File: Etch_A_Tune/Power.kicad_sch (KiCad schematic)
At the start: 2 parts, among them IC4 LM2775DSGR, IC5 TPS62063DSGR

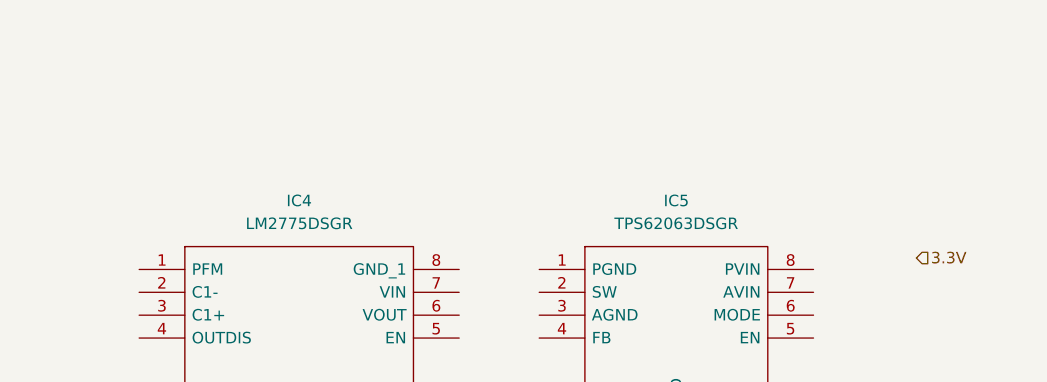
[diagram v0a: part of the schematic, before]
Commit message: Updated schematic and preliminary PCB doc
did rough PCB layout
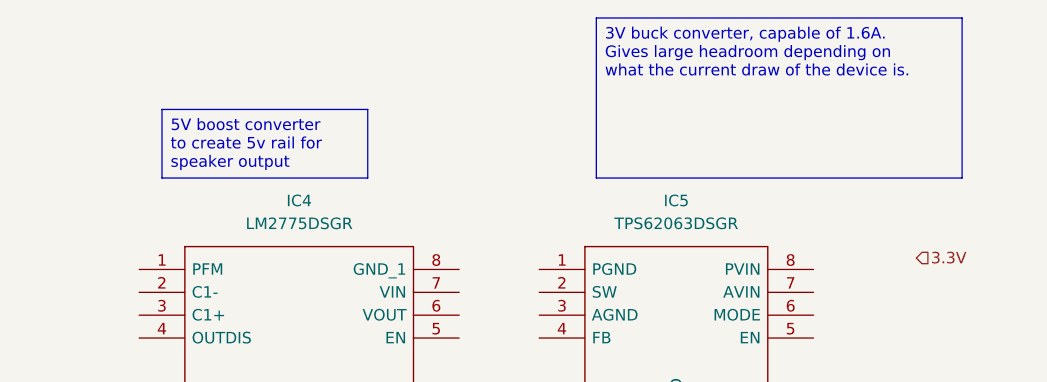
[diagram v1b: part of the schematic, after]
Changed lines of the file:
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@@
 	(generator_version "9.0")
 	(paper "A4")
+	(text_box "3V buck converter, capable of 1.6A. Gives large headroom depending on what the current draw of the device is.\n"
+		(exclude_from_sim no)
+		(at 190.5 50.8 0)
+		(size 40.64 17.78)
+		(margins 0.9525 0.9525 0.9525 0.9525)
+		(stroke
+			(width 0)
+			(type solid)
+		)
+		(fill
+			(type none)
+		)
+		(effects
+			(font
+				(size 1.27 1.27)
+			)
+			(justify left top)
+		)
+	)
+	(text_box "5V boost converter to create 5v rail for speaker output\n"
+		(exclude_from_sim no)
+		(at 142.24 60.96 0)
+		(size 22.86 7.62)
+		(margins 0.9525 0.9525 0.9525 0.9525)
+		(stroke
+			(width 0)
+			(type solid)
+		)
+		(fill
+			(type none)
+		)
+		(effects
+			(font
+				(size 1.27 1.27)
+			)
+			(justify left top)
+		)
+	)
 	(hierarchical_label "3.3V"
 		(shape input)

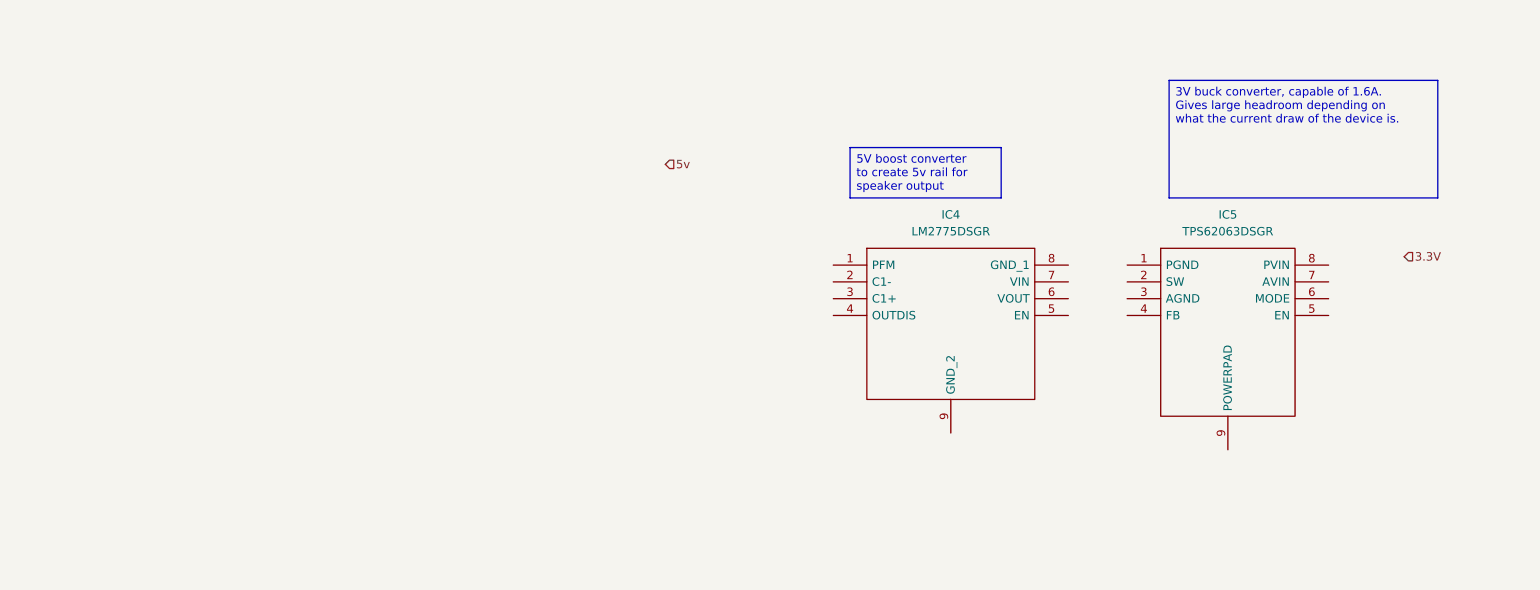
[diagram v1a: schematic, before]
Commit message: Schematic Update
Fixed component Footprints and added new switches/rotary encoders. Wired and placed bypass capacitors for most devices. Removed 5V boost converter because external DAC is no longer being utilized. Placed uC onto board design and implemented charging through USB-C connector.
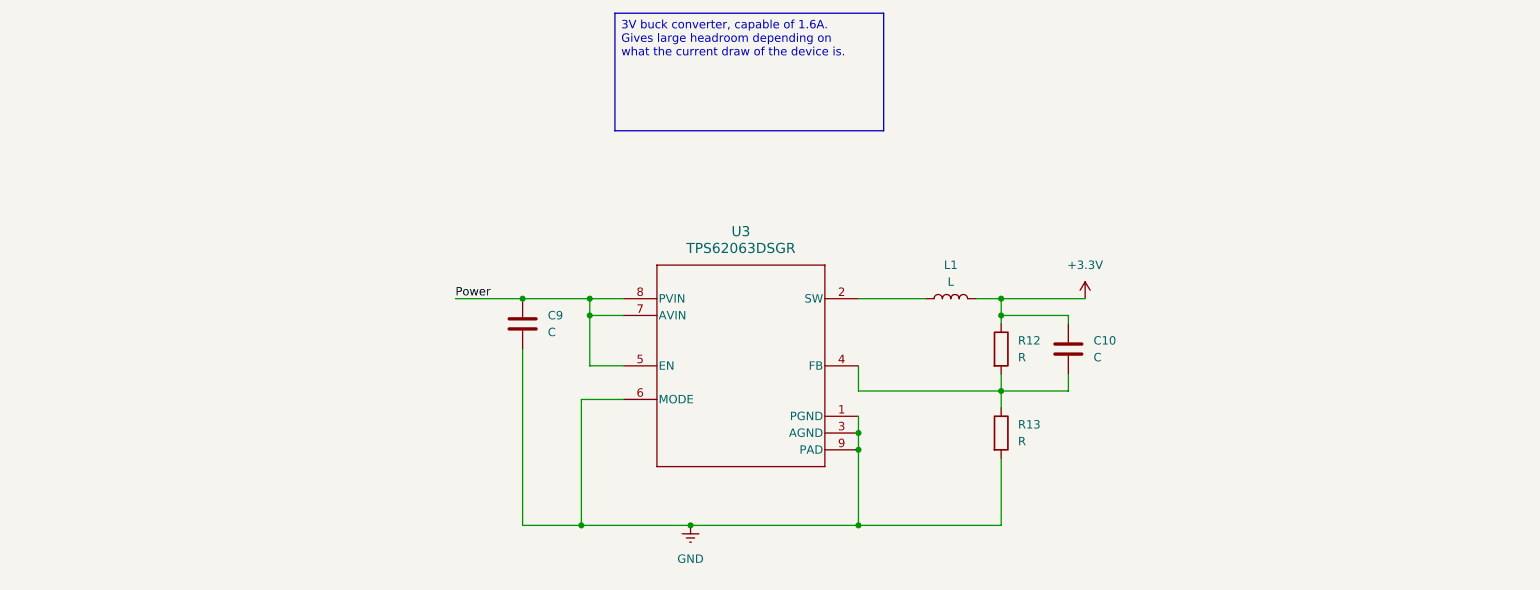
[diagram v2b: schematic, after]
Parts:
- removed IC4: LM2775DSGR, SON50P200X200X80-9N, symbol SamacSys_Parts:LM2775DSGR
- removed IC5: TPS62063DSGR, SON50P200X200X80-9N, symbol SamacSys_Parts:TPS62063DSGR
- added C10, C9: C, symbol Device:C
- added L1: L, symbol Device:L
- added R12, R13: R, symbol Device:R
- added U3: TPS62063DSGR, BQ25170DSGR:DSG0008A, symbol TPS62063DSGR:TPS62063DSGR
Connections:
- new net: L1.1, U3.2 (SW)
- new net: C10.2, R12.2, R13.1, U3.4 (FB)
- new net +3.3V: C10.1, L1.2, R12.1
- new net GND: C9.2, R13.2, U3.1 (PGND), U3.3 (AGND), U3.6 (MODE), U3.9 (PAD)
- new net Power: C9.1, U3.5 (EN), U3.7 (AVIN), U3.8 (PVIN)

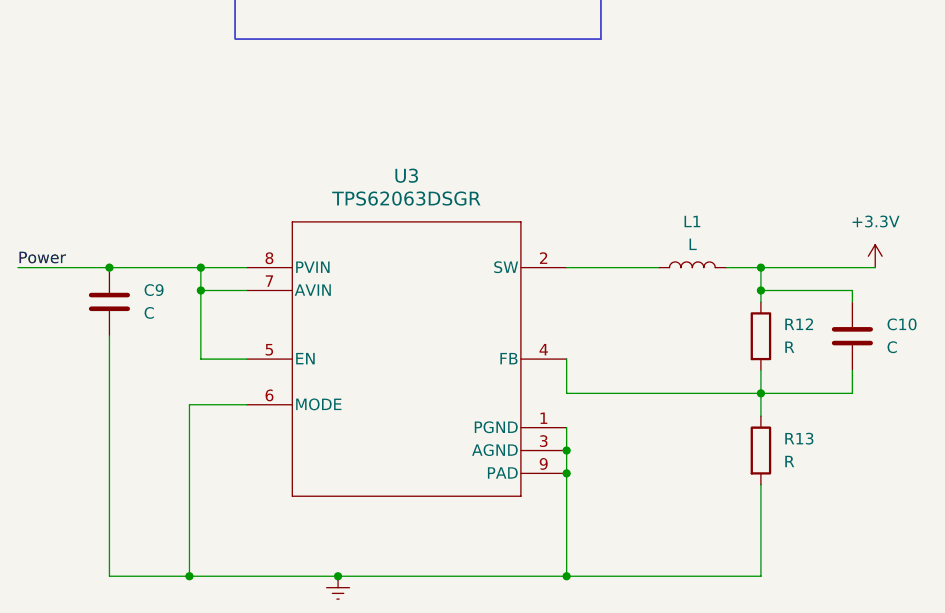
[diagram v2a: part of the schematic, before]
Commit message: Etch A Tune V.02
Updated more foot prints and components onto bom, specifically SWD debug header and 1x14 pin header for touch and screen module. Added 4pin header for SD card reader.
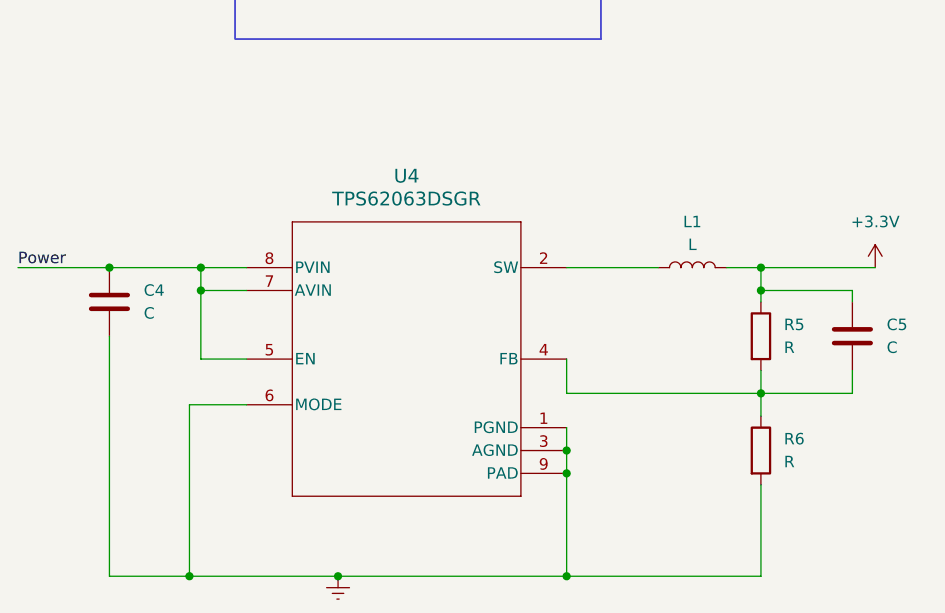
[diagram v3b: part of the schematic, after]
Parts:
- renumbered C9 to C4, C10 to C5, R12 to R5, R13 to R6, U3 to U4
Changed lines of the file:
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@@
 		(dnp no)
 		(fields_autoplaced yes)
-		(property "Reference" "C9"
+		(property "Reference" "C4"
 			(at 96.52 86.3599 0)
 			(effects
@@
 			(project "Etch_A_Tune"
 				(path "/b4cdadf2-c4fe-48fe-ba6a-e15d1cad03b2/e5e22929-d6f1-4829-905c-a53e6965babb"
-					(reference "C9")
+					(reference "C4")
 					(unit 1)
 				)
@@
 		(dnp no)
 		(fields_autoplaced yes)
-		(property "Reference" "U3"
+		(property "Reference" "U4"
 			(at 125.73 73.66 0)
 			(effects
@@
 			(project ""
 				(path "/b4cdadf2-c4fe-48fe-ba6a-e15d1cad03b2/e5e22929-d6f1-4829-905c-a53e6965babb"
-					(reference "U3")
+					(reference "U4")
 					(unit 1)
 				)
@@
 		(dnp no)
 		(fields_autoplaced yes)
-		(property "Reference" "#PWR016"
+		(property "Reference" "#PWR08"
 			(at 118.11 124.46 0)
 			(effects
@@
 			(project "Etch_A_Tune"
 				(path "/b4cdadf2-c4fe-48fe-ba6a-e15d1cad03b2/e5e22929-d6f1-4829-905c-a53e6965babb"
-					(reference "#PWR016")
+					(reference "#PWR08")
 					(unit 1)
 				)
@@
 		(dnp no)
 		(fields_autoplaced yes)
-		(property "Reference" "R12"
+		(property "Reference" "R5"
 			(at 167.64 90.1699 0)
 			(effects
@@
 			(project "Etch_A_Tune"
 				(path "/b4cdadf2-c4fe-48fe-ba6a-e15d1cad03b2/e5e22929-d6f1-4829-905c-a53e6965babb"
-					(reference "R12")
+					(reference "R5")
 					(unit 1)
 				)
@@
 		(dnp no)
 		(fields_autoplaced yes)
-		(property "Reference" "R13"
+		(property "Reference" "R6"
 			(at 167.64 102.8699 0)
 			(effects
@@
 			(project "Etch_A_Tune"
 				(path "/b4cdadf2-c4fe-48fe-ba6a-e15d1cad03b2/e5e22929-d6f1-4829-905c-a53e6965babb"
-					(reference "R13")
+					(reference "R6")
 					(unit 1)
 				)
@@
 		(dnp no)
 		(fields_autoplaced yes)
-		(property "Reference" "#PWR04"
+		(property "Reference" "#PWR09"
 			(at 177.8 87.63 0)
 			(effects
@@
 			(project "Etch_A_Tune"
 				(path "/b4cdadf2-c4fe-48fe-ba6a-e15d1cad03b2/e5e22929-d6f1-4829-905c-a53e6965babb"
-					(reference "#PWR04")
+					(reference "#PWR09")
 					(unit 1)
 				)
@@
 		(dnp no)
 		(fields_autoplaced yes)
-		(property "Reference" "C10"
+		(property "Reference" "C5"
 			(at 179.07 90.1699 0)
 			(effects
@@
 			(project "Etch_A_Tune"
 				(path "/b4cdadf2-c4fe-48fe-ba6a-e15d1cad03b2/e5e22929-d6f1-4829-905c-a53e6965babb"
-					(reference "C10")
-					(unit 1)
-				)
+					(reference "C5")
+					(unit 1)
+				)

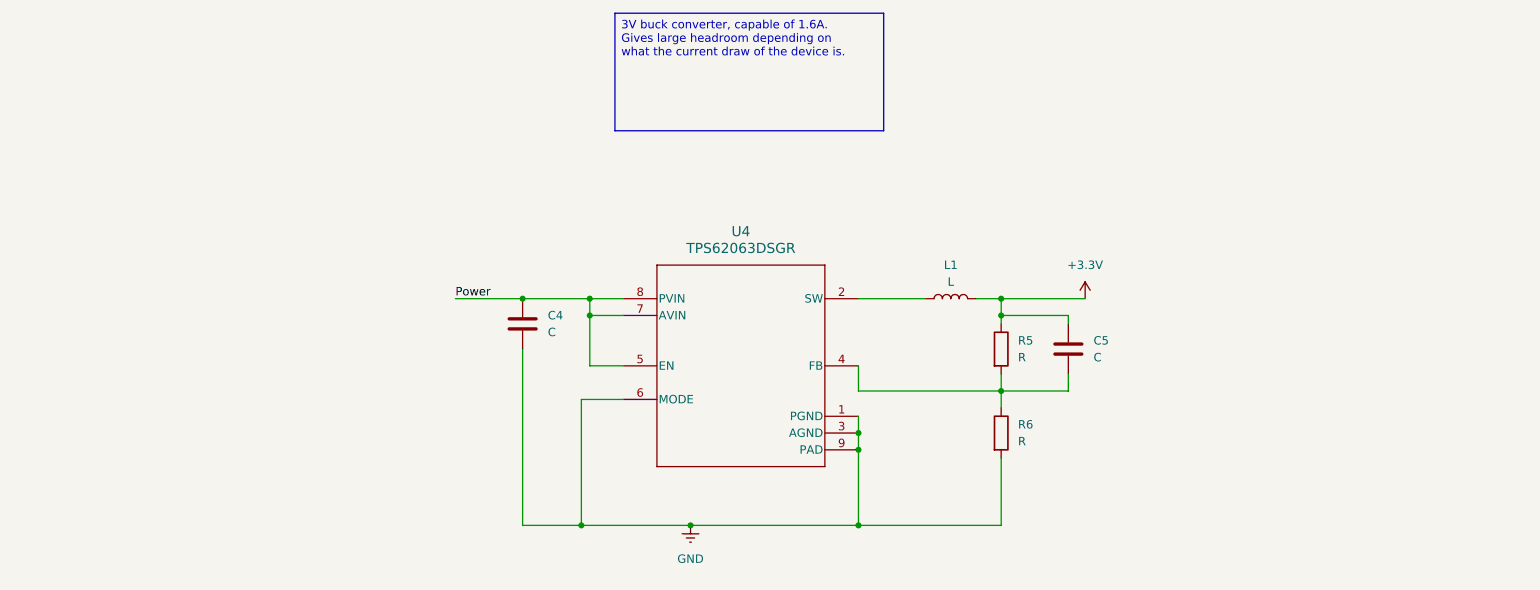
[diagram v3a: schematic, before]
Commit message: Updated parallel power supply
Updated USB and battery operation and added DAC output
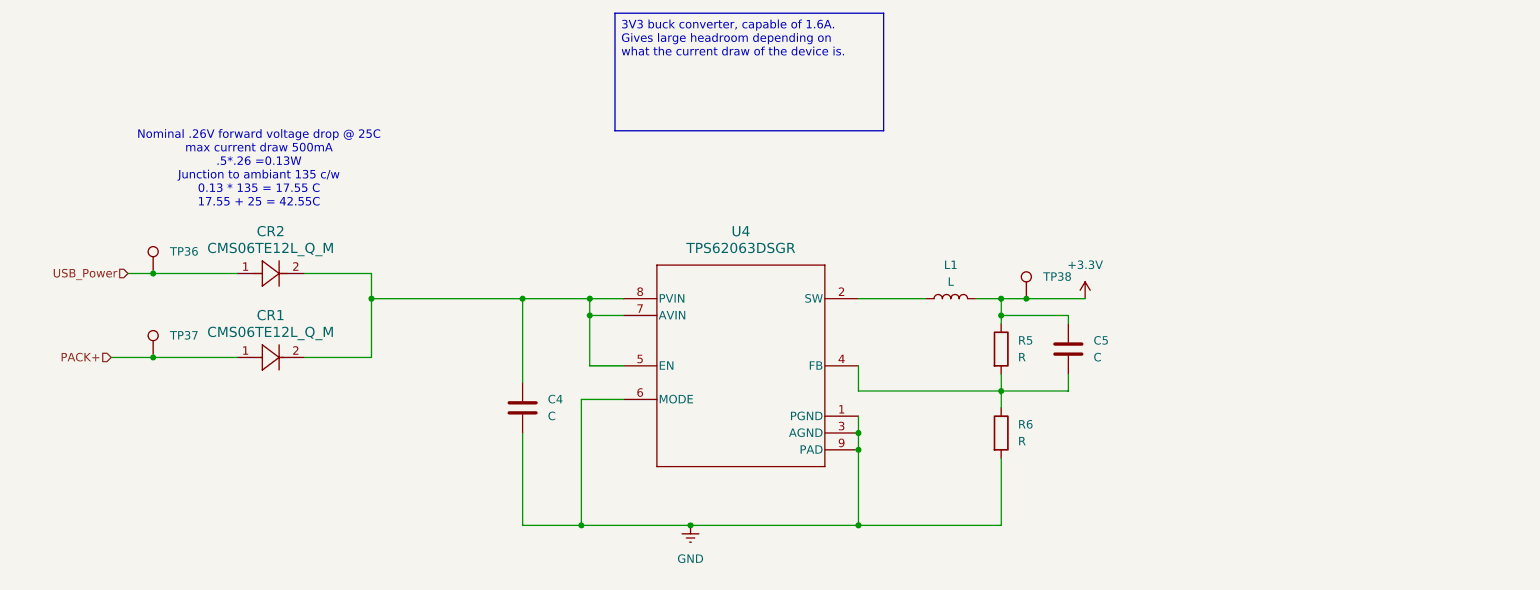
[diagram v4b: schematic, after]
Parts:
- added CR1, CR2: CMS06TE12L_Q_M, BQ25170DSGR:M-FLAT_TOS-L, symbol CMS06(TE12L,Q,M):CMS06TE12L_Q_M
- added TP36, TP37, TP38: TestPoint, TestPoint:TestPoint_Pad_D1.0mm, symbol Connector:TestPoint
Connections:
- net +3.3V: now also TP38.1
- net Power: no longer names the net of C4.1, U4.5 (EN), U4.7 (AVIN), U4.8 (PVIN)
- net Power: now also CR1.2, CR2.2
- new net PACK+: CR1.1, TP37.1
- new net USB_Power: CR2.1, TP36.1
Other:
- note added: "Nominal .26V forward voltage drop @ 25C max current draw 500mA .5*.26 =0.13W Junction to ambiant 135 c/w 0.13 * 135 = 17.55 C 17.55 + 25 = 42.55C"
- moved on the sheet: C4

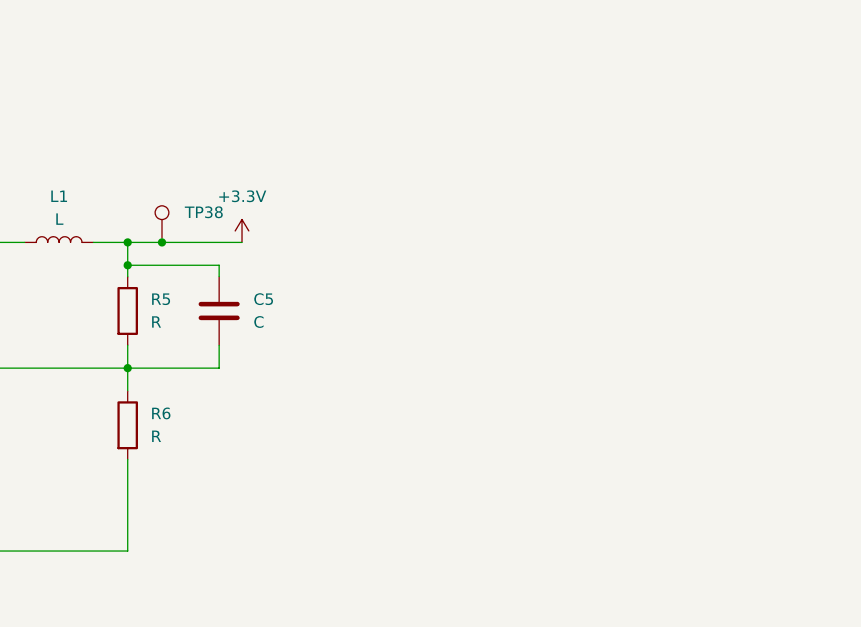
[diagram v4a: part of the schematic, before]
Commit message: V.04 Schematic
added 64 pin header LEDS
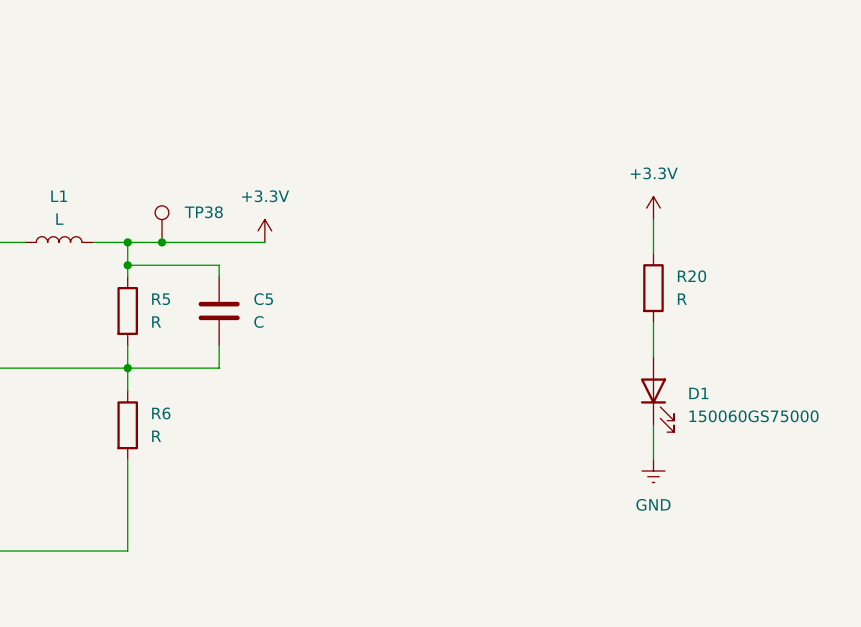
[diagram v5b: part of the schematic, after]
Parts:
- added D1: 150060GS75000, symbol Device:LED
- added R20: R, symbol Device:R
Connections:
- net +3.3V: now also R20.1
- net GND: now also D1.1 (K)
- new net: D1.2 (A), R20.2

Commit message: Final Layout before routing
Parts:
- added C9: 10uF, Capacitor_SMD:C_0603_1608Metric, symbol Device:C
- added R27, R29, R30: 0, Resistor_SMD:R_0603_1608Metric, symbol Device:R
- C4: value C -> 10uF; footprint (none) -> Capacitor_SMD:C_0603_1608Metric
- C5: value C -> 22pF; footprint (none) -> Capacitor_SMD:C_0603_1608Metric
- D1: footprint (none) -> LED_SMD:LED_0603_1608Metric
- L1: value L -> 1UH; footprint (none) -> Inductor_SMD:L_1210_3225Metric
- R20: value R -> 10; footprint (none) -> Resistor_SMD:R_0603_1608Metric
- R5: value R -> 360k; footprint (none) -> Resistor_SMD:R_0603_1608Metric
- R6: value R -> 180k; footprint (none) -> Resistor_SMD:R_0603_1608Metric
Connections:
- net +3.3V: now also C9.1, R30.2; no longer C5.1, L1.2, R5.1, TP38.1
- net GND: now also C9.2
- net PACK+: now also R27.1; no longer CR1.1
- net USB_Power: now also R29.1; no longer CR2.1
- new net: CR2.1, R29.2
- new net: C5.1, L1.2, R30.1, R5.1, TP38.1
- new net: CR1.1, R27.2
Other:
- moved on the sheet: TP36, TP37
